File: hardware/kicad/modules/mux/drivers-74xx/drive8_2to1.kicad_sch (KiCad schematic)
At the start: 8 parts, among them U1 74AHC541, U2 74AHC541

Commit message: module: designed muxes prioritizing drivers for large switching preserving depth of ~1 gate
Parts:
- removed C2, C3, C4, C5: 100nF, Capacitor_SMD:C_0603_1608Metric, symbol Device:C
- added C158: 100nF, Capacitor_SMD:C_0603_1608Metric, symbol Device:C
- added U160: 74AHC1G04, Package_TO_SOT_SMD:SOT-23-5, symbol 74xGxx:74AHC1G04
- U159: renamed from U1; footprint Package_SO:SSOP-20_4.4x6.5mm_P0.65mm -> Package_SO:SOIC-20W_7.5x12.8mm_P1.27mm
- U161: renamed from U2; footprint Package_SO:SSOP-20_4.4x6.5mm_P0.65mm -> Package_SO:SOIC-20W_7.5x12.8mm_P1.27mm
- renumbered C1 to C157, C6 to C159
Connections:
- net GND: now also C158.1, U160.3 (GND)
- net VCC: now also C158.2, U160.5 (VCC)
- net sel: now reaches U159.1 (G1)
- net sel: now also U159.19 (G2), U160.2
- net ~en: now reaches U161.1 (G1)
- net ~en: now also U161.19 (G2), U160.4

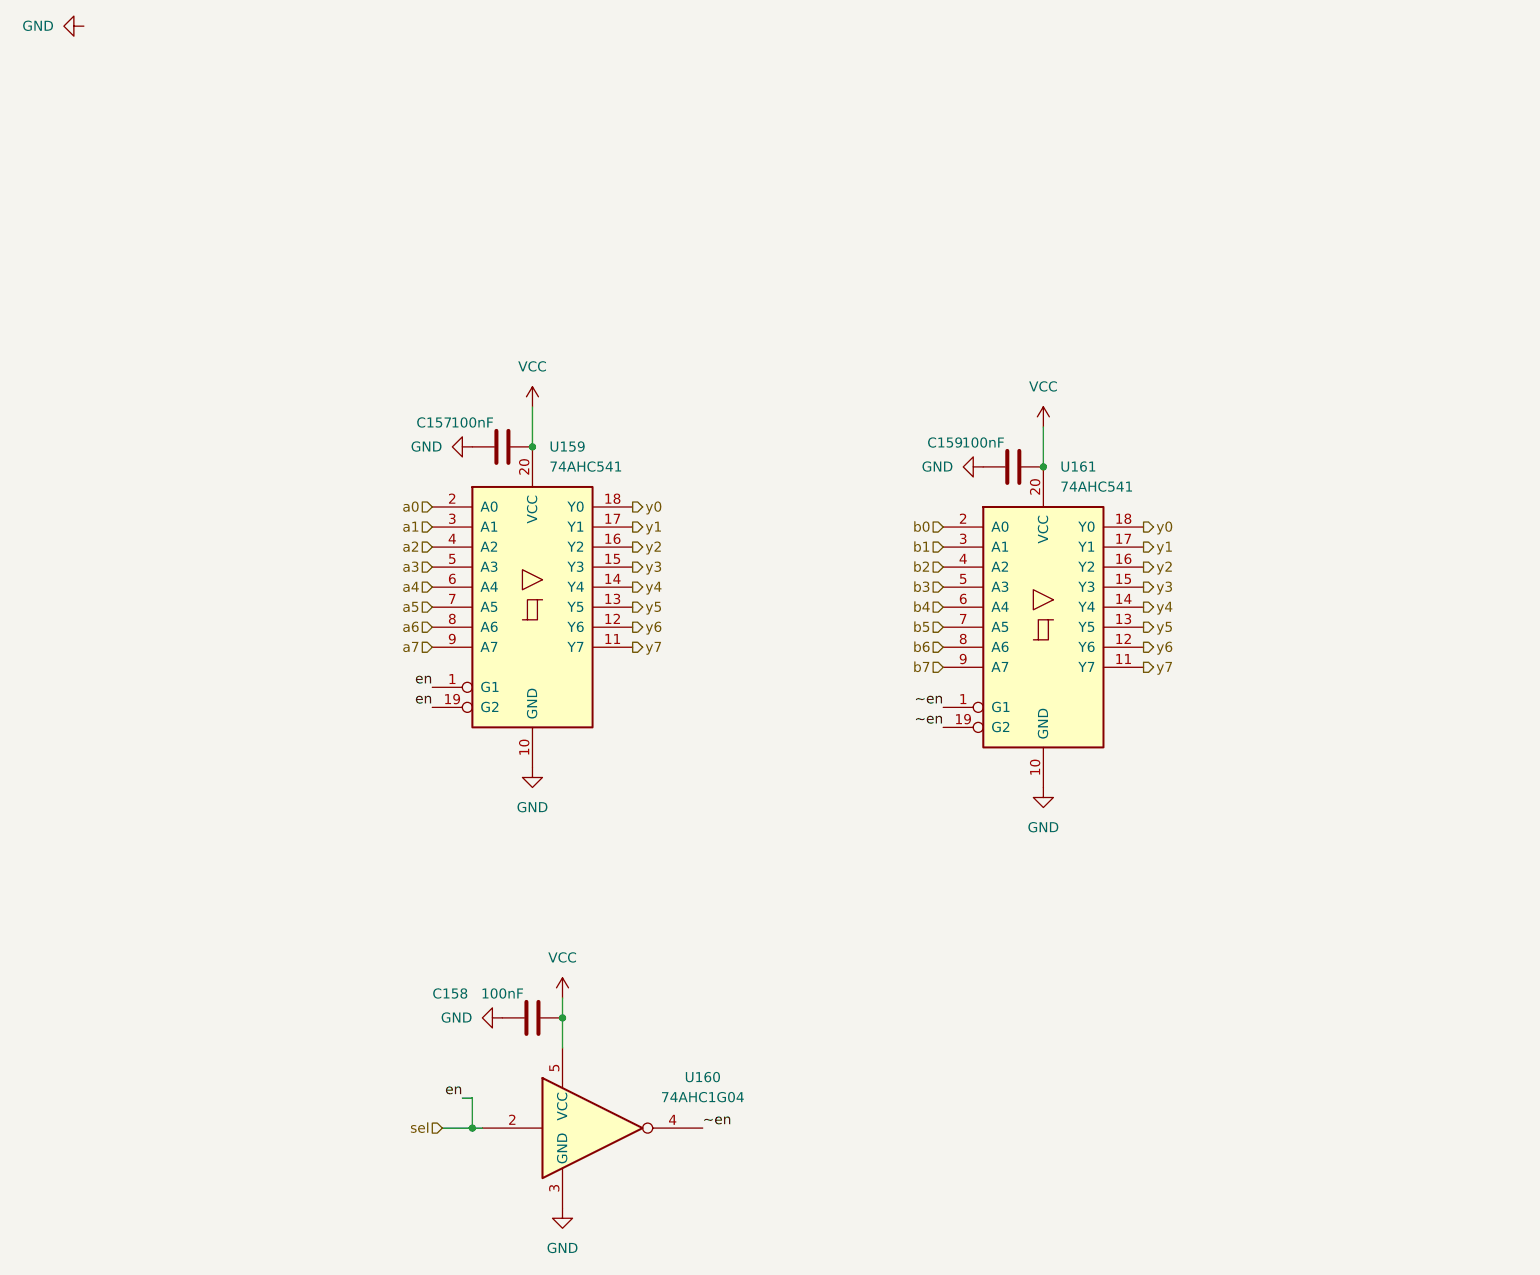
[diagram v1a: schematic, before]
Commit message: refactor: improved driver with data bus for readability
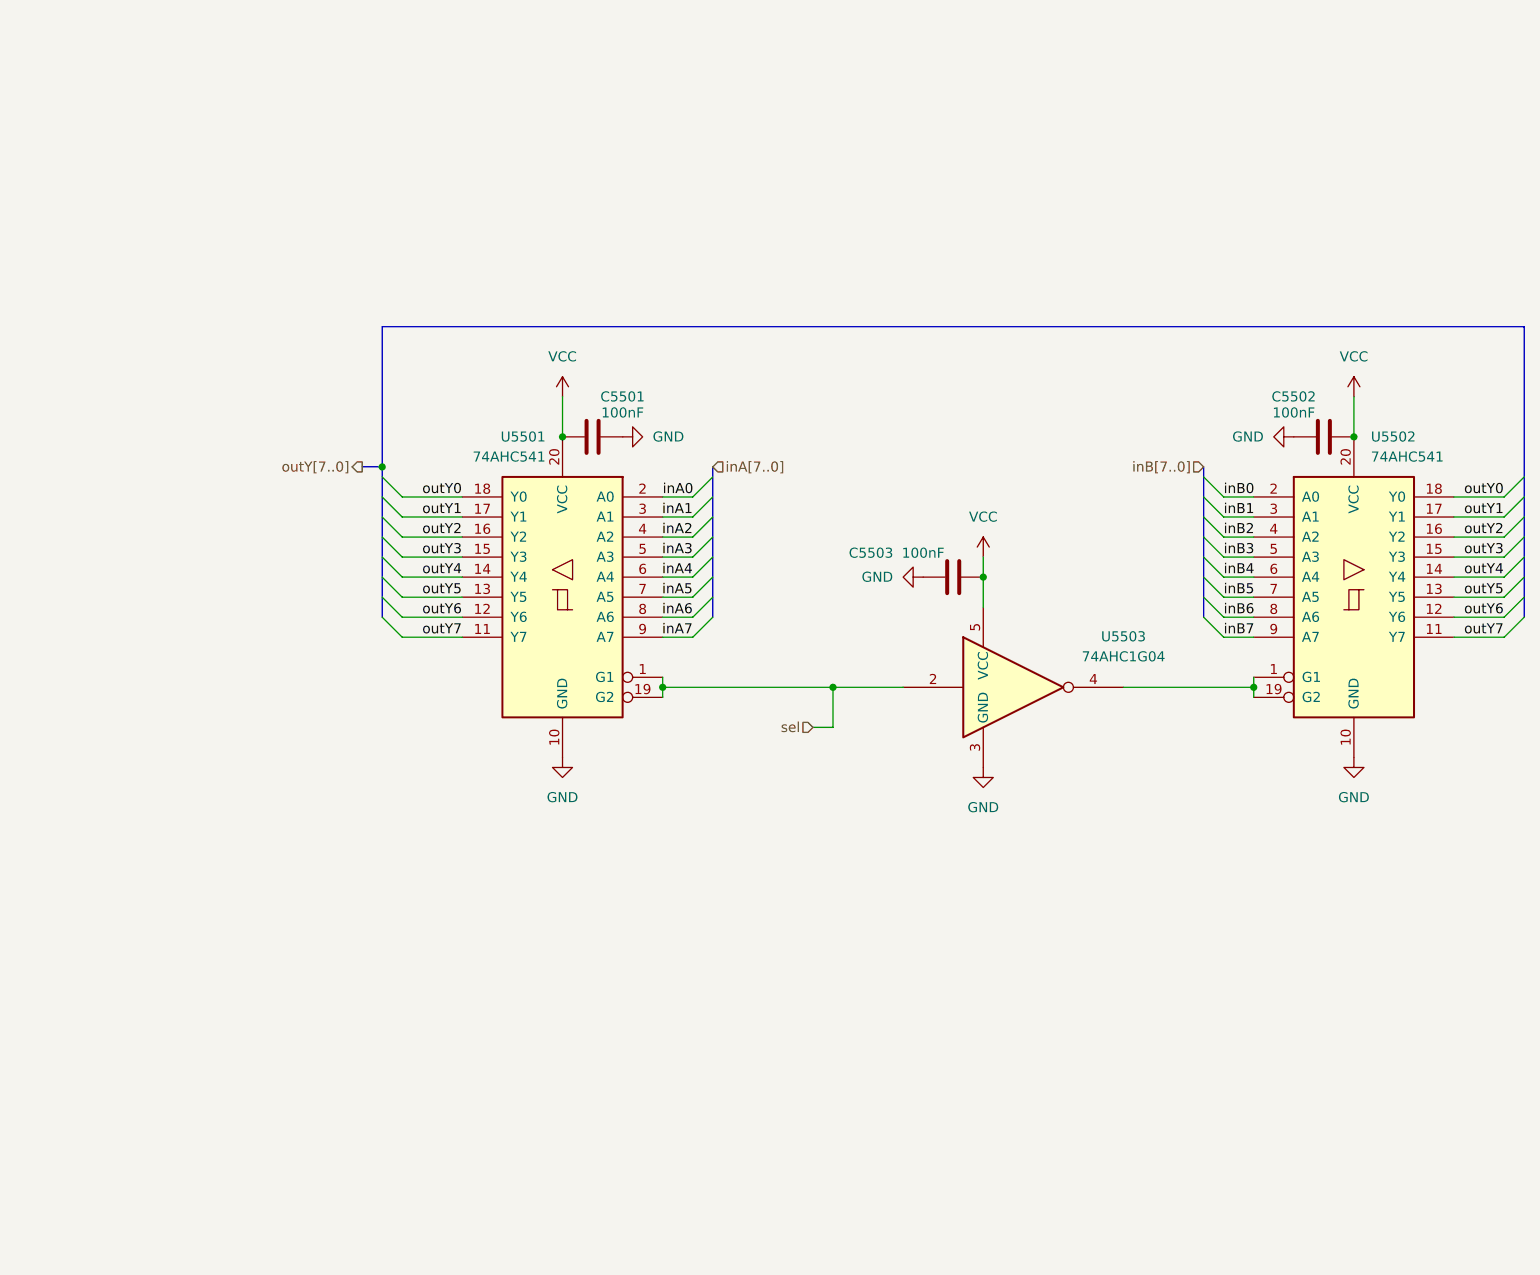
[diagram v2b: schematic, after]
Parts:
- removed C159: 100nF, Capacitor_SMD:C_0603_1608Metric, symbol Device:C
- removed U161: 74AHC541, Package_SO:SOIC-20W_7.5x12.8mm_P1.27mm, symbol 74xx:74AHC541
- added C5502: 100nF, Capacitor_SMD:C_0603_1608Metric, symbol Device:C
- added U5502: 74AHC541, Package_SO:SOIC-20W_7.5x12.8mm_P1.27mm, symbol 74xx:74AHC541
- renumbered C157 to C5501, C158 to C5503, U159 to U5501, U160 to U5503
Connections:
- net GND: now also C5502.1, U5502.10 (GND)
- net VCC: now also C5502.2, U5502.20 (VCC)
- net a0 renamed inA0
- net a1 renamed inA1
- net a2 renamed inA2
- net a3 renamed inA3
- net a4 renamed inA4
- net a5 renamed inA5
- net a6 renamed inA6
- net a7 renamed inA7
- net y0 renamed outY0
- net outY0: now also U5502.18 (Y0)
- net y1 renamed outY1
- net outY1: now also U5502.17 (Y1)
- net y2 renamed outY2
- net outY2: now also U5502.16 (Y2)
- net y3 renamed outY3
- net outY3: now also U5502.15 (Y3)
- net y4 renamed outY4
- net outY4: now also U5502.14 (Y4)
- net y5 renamed outY5
- net outY5: now also U5502.13 (Y5)
- net y6 renamed outY6
- net outY6: now also U5502.12 (Y6)
- net y7 renamed outY7
- net outY7: now also U5502.11 (Y7)
- net ~en: no longer names the net of U5503.4
- net ~en: now also U5502.1 (G1), U5502.19 (G2)
- new net inB0: U5502.2 (A0)
- new net inB1: U5502.3 (A1)
- new net inB2: U5502.4 (A2)
- new net inB3: U5502.5 (A3)
- new net inB4: U5502.6 (A4)
- new net inB5: U5502.7 (A5)
- new net inB6: U5502.8 (A6)
- new net inB7: U5502.9 (A7)
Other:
- moved on the sheet: C5501, C5503, U5501, U5503

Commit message: arch: added LEDs, override switches; fixed errors and warnings to 0
ready for routing after logical coherence check
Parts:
- renumbered C5501 to C156, C5503 to C157, C5502 to C158, U5501 to U156, U5503 to U157, U5502 to U158

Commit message: chore: modified muxes that alu depends on
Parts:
- renumbered C156 to C161, C157 to C162, C158 to C163, U156 to U161, U157 to U162, U158 to U163

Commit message: chore: power flag annotation on independent h-sheets
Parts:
- renumbered C161 to C93, C163 to C94, C162 to C95, U161 to U71, U163 to U72, U162 to U73
